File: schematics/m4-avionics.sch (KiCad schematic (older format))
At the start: 7 parts

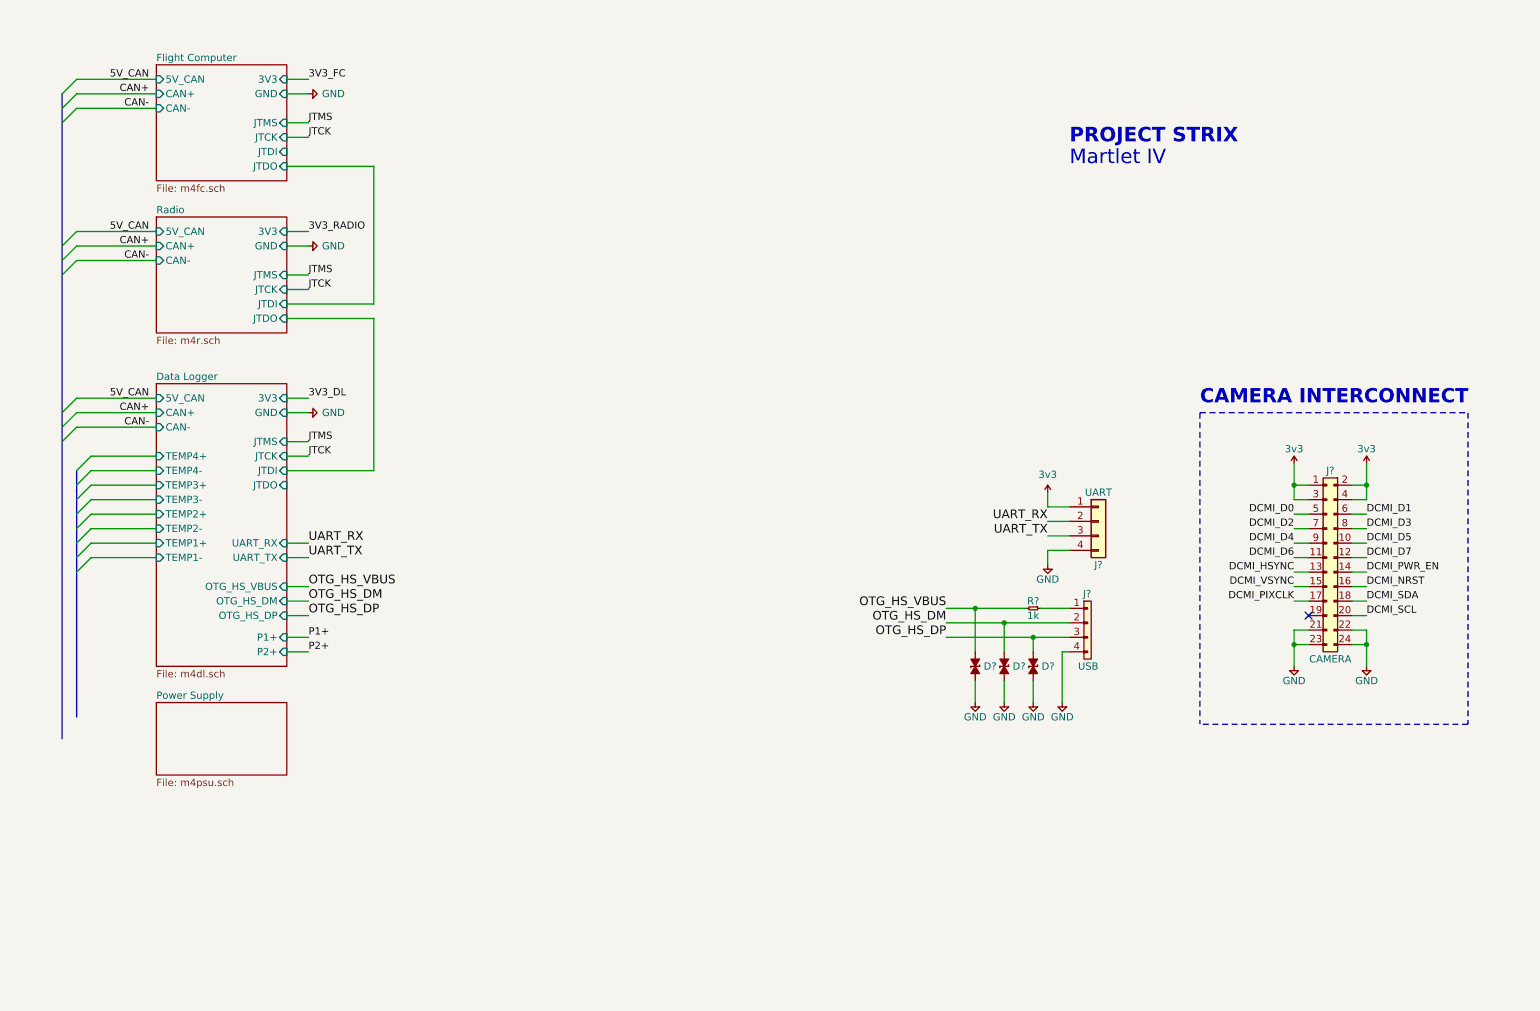
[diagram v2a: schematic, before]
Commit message: Add master microcontroller
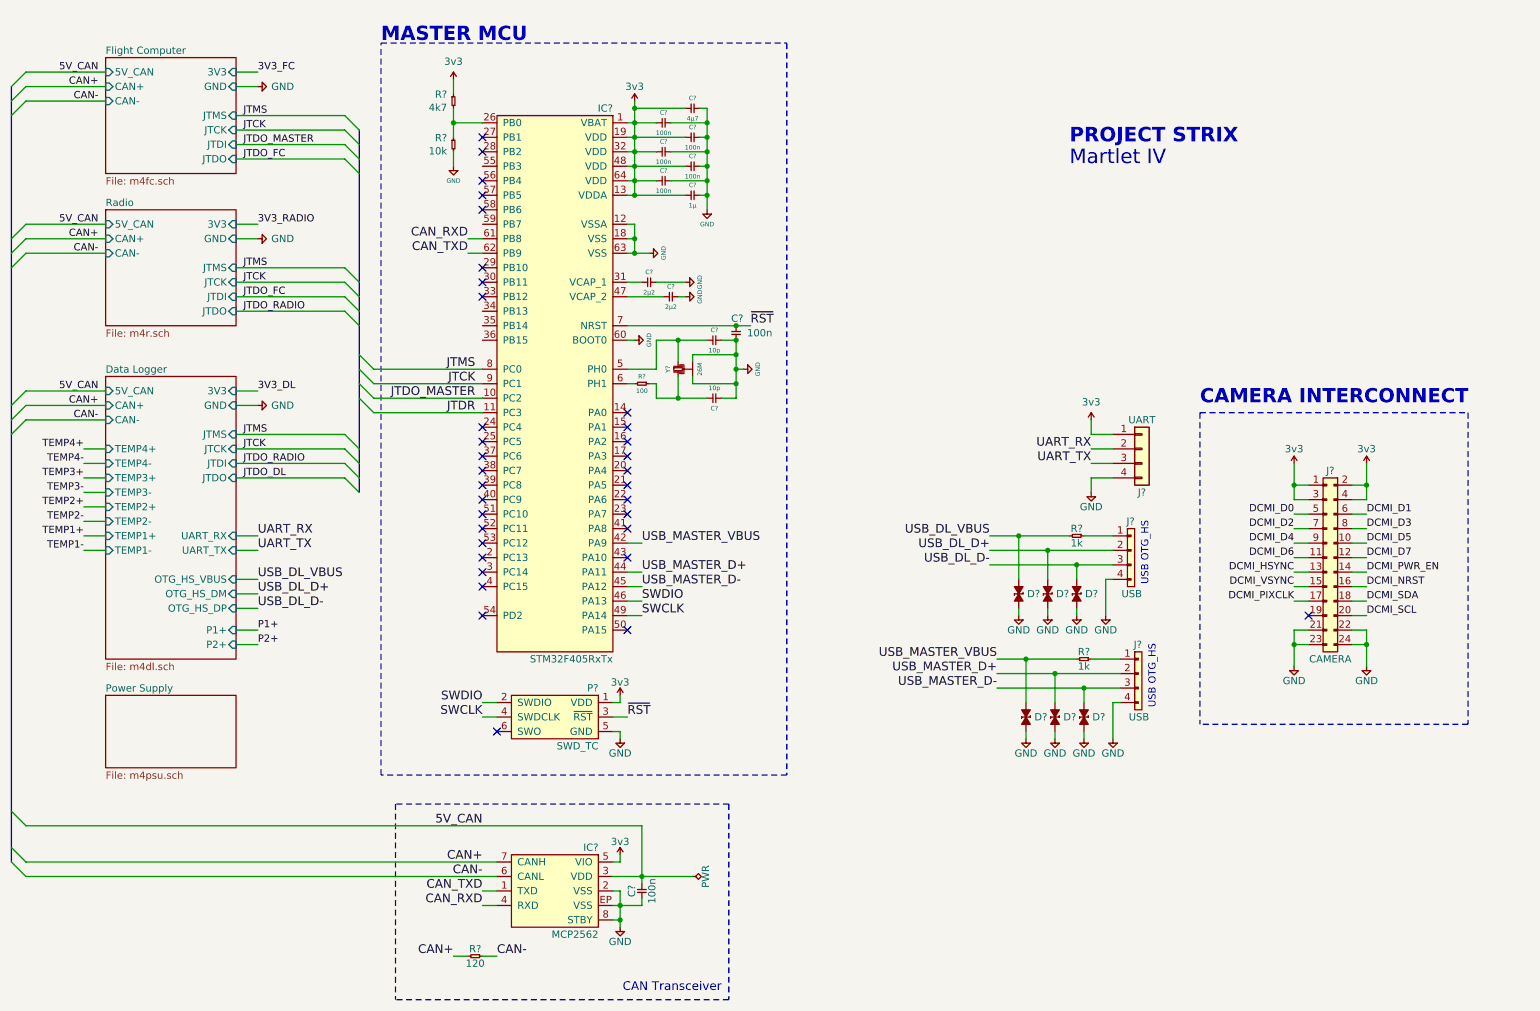
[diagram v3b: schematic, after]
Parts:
- added C? (x2): 10p, agg:0402, symbol cusf-kicad:C
- added C?: 1µ, agg:0402, symbol cusf-kicad:C
- added C?: 4µ7, agg:0402, symbol cusf-kicad:C
- added C? (x6): 100n, agg:0402, symbol cusf-kicad:C
- added C? (x2): 2µ2, agg:0402, symbol cusf-kicad:C
- added C?: 100n, symbol cusf-kicad:C
- added D? (x3): ESD_DIODE, cusf:0402, symbol cusf-kicad:ESD_DIODE
- added IC?: STM32F405RxTx, agg:LQFP-64, symbol cusf-kicad:STM32F405RxTx
- added IC?: MCP2562, agg:DFN-8-EP-MICROCHIP, symbol cusf-kicad:MCP2562
- added J?: USB, Connectors_Molex:Connector_Molex_PicoBlade_53261-0471, symbol cusf-kicad:CONN_01x04
- added P?: SWD_TC, agg:TC2030-NL, symbol cusf-kicad:SWD_TC
- added R?: 100, agg:0402, symbol cusf-kicad:R
- added R?: 120, agg:0603, symbol cusf-kicad:R
- added R?: 10k, symbol cusf-kicad:R
- added R?: 4k7, symbol cusf-kicad:R
- added R?: 1k, symbol cusf-kicad:R
- added Y?: 26M, agg:XTAL-20x16, symbol cusf-kicad:SMD_XTAL
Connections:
- net 3v3: now also C?.2, C?.2, C?.2, C?.2, C?.2, C?.2, C?.2, IC?.1 (VBAT), IC?.13 (VDDA), IC?.19 (VDD), IC?.32 (VDD), IC?.48 (VDD), IC?.5 (VIO), IC?.64 (VDD), P?.1 (VDD), R?.1
- net 5V_CAN: now also C?.1, IC?.3 (VDD)
- net CAN+: now also IC?.7 (CANH), R?.2
- net CAN-: now also IC?.6 (CANL), R?.1
- net GND: now also C?.1, C?.1, C?.1, C?.1, C?.1, C?.1, C?.1, C?.1, C?.1, C?.2, C?.2, C?.2, C?.2, D?.2, D?.2, D?.2, IC?.12 (VSSA), IC?.18 (VSS), IC?.2 (VSS), IC?.60 (BOOT0), IC?.63 (VSS), IC?.8 (STBY), IC?.EP (VSS), J?.4, P?.5 (GND), R?.2, Y?.2, Y?.4
- net JTCK: now also IC?.9 (PC1)
- net JTMS: now also IC?.8 (PC0)
- net OTG_HS_DM renamed USB_DL_D+
- net OTG_HS_DP renamed USB_DL_D-
- net OTG_HS_VBUS renamed USB_DL_VBUS
- new net: IC?.26 (PB0), R?.1, R?.2
- new net: C?.1, IC?.31 (VCAP_1)
- new net: C?.1, IC?.47 (VCAP_2)
- new net: C?.2, IC?.5 (PH0), Y?.1
- new net: IC?.6 (PH1), R?.2
- new net: C?.2, R?.1, Y?.3
- new net: J?.1, R?.1
- new net CAN_RXD: IC?.4 (RXD), IC?.61 (PB8)
- new net CAN_TXD: IC?.1 (TXD), IC?.62 (PB9)
- new net JTDO_MASTER: IC?.10 (PC2)
- new net JTDR: IC?.11 (PC3)
- new net SWCLK: IC?.49 (PA14), P?.4 (SWDCLK)
- new net SWDIO: IC?.46 (PA13), P?.2 (SWDIO)
- new net USB_MASTER_D+: D?.1, IC?.44 (PA11), J?.2
- new net USB_MASTER_D-: D?.1, IC?.45 (PA12), J?.3
- new net USB_MASTER_VBUS: D?.1, IC?.42 (PA9), R?.2
- new net ~RST: C?.1, IC?.7 (NRST), P?.3 (~RST)
- no-connect marks 1 -> 34
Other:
- note added: "CAN Transceiver"
- note added: "MASTER MCU"
- note added: "USB OTG_HS"
- moved on the sheet: D?, J?, R?

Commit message: Master layout reorganisation and cleanup
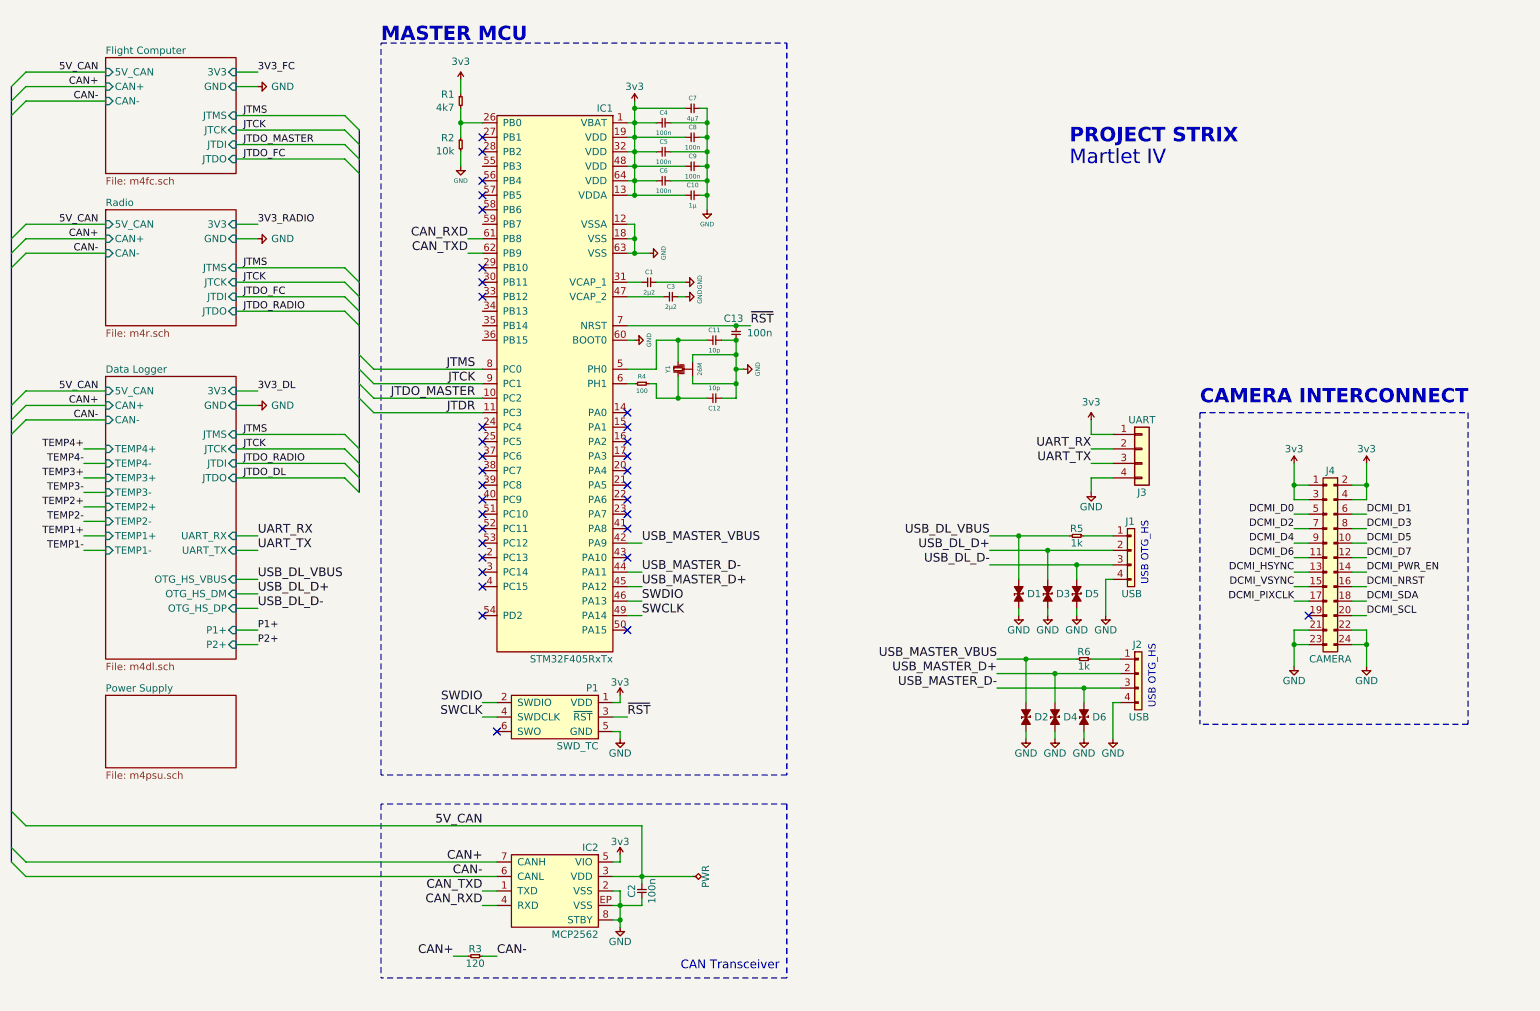
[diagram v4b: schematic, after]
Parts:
- gave numbers to parts that had none: 33
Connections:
- net USB_MASTER_D+: now also IC1.45 (PA12); no longer IC1.44 (PA11)
- net USB_MASTER_D-: now also IC1.44 (PA11); no longer IC1.45 (PA12)
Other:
- moved on the sheet: R1, R2

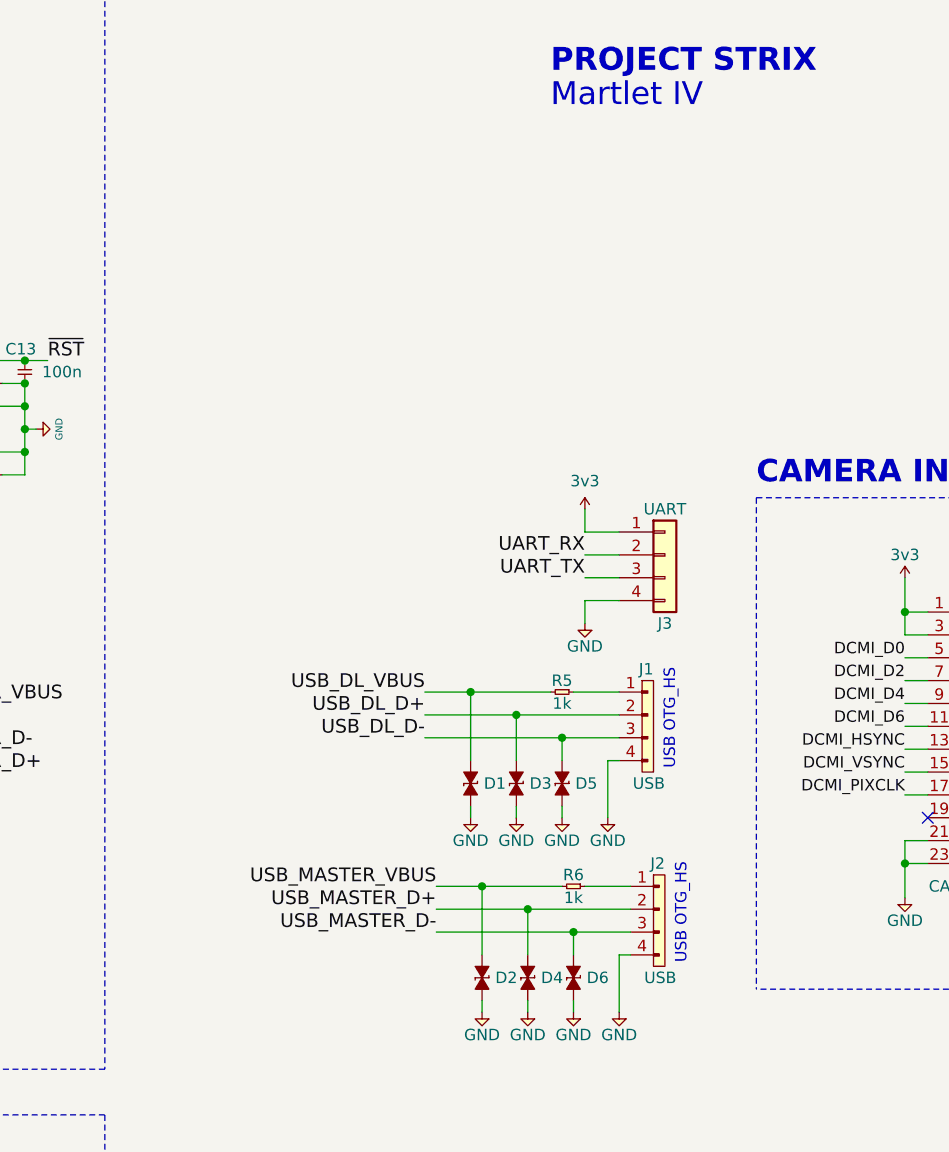
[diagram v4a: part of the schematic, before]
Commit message: Add dummy thermocouple and pressure connectors
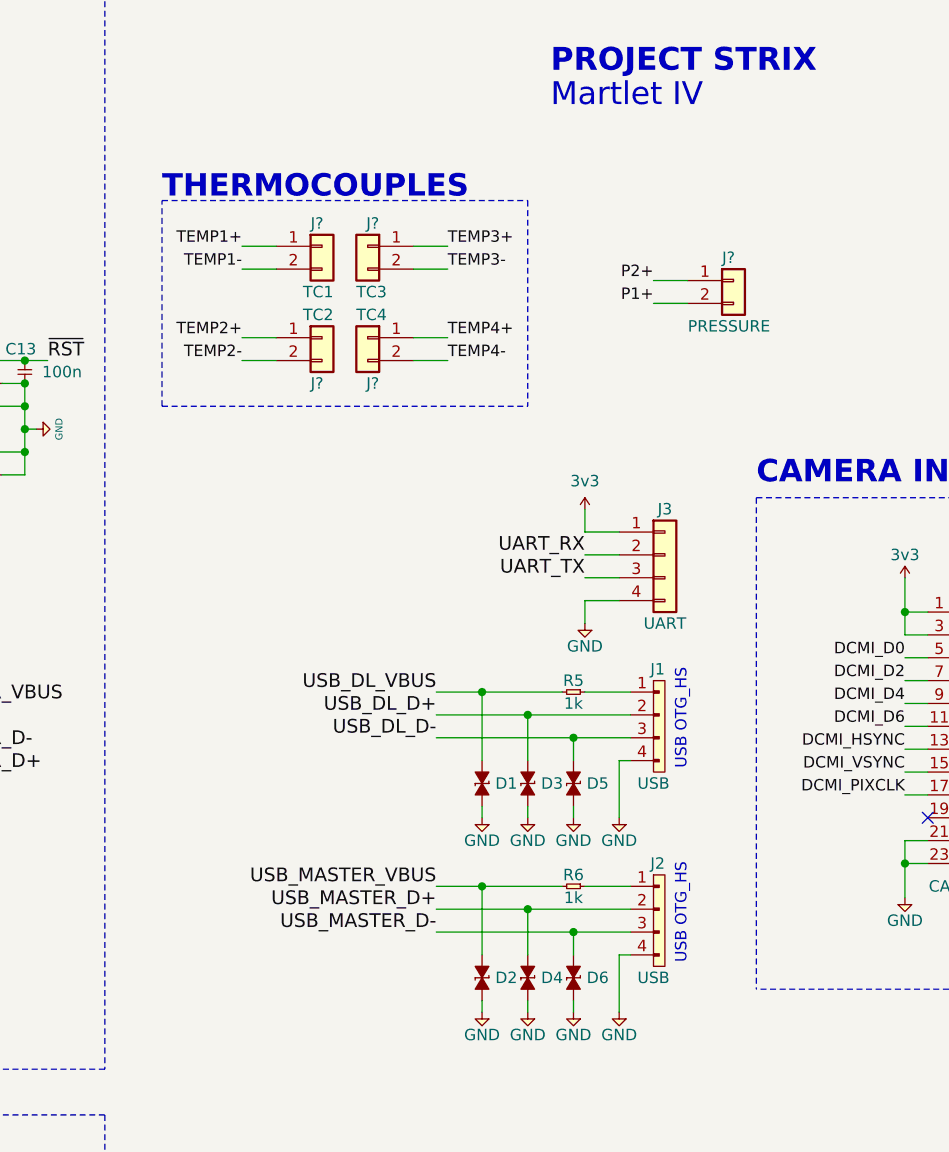
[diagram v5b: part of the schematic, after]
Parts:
- added J?: PRESSURE, symbol Connector_Generic:Conn_01x02
- added J?: TC1, symbol Connector_Generic:Conn_01x02
- added J?: TC2, symbol Connector_Generic:Conn_01x02
- added J?: TC3, symbol Connector_Generic:Conn_01x02
- added J?: TC4, symbol Connector_Generic:Conn_01x02
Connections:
- net P1+: now also J?.2 (Pin_2)
- net P2+: now also J?.1 (Pin_1)
- net TEMP1+: now also J?.1 (Pin_1)
- net TEMP1-: now also J?.2 (Pin_2)
- net TEMP2+: now also J?.1 (Pin_1)
- net TEMP2-: now also J?.2 (Pin_2)
- net TEMP3+: now also J?.1 (Pin_1)
- net TEMP3-: now also J?.2 (Pin_2)
- net TEMP4+: now also J?.1 (Pin_1)
- net TEMP4-: now also J?.2 (Pin_2)
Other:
- note added: "THERMOCOUPLES"
- moved on the sheet: D1, D3, D5, J1, R5

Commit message: Improve thermocouple and pressure connectors
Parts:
- added J?: PRESSURE_2, symbol Connector_Generic:Conn_01x04
- J?: value PRESSURE -> PRESSURE_1; symbol Connector_Generic:Conn_01x02 -> Connector_Generic:Conn_01x04
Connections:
- net P1+: now also J?.3 (Pin_3); no longer J?.2 (Pin_2)
- net P2+: now also J?.3 (Pin_3); no longer J?.1 (Pin_1)
- no-connect marks 34 -> 36
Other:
- note added: "PRESSURE CONN"
- moved on the sheet: D1, D2, D3, D4, D5, D6, J1, J2, J3, J?, R5, R6
